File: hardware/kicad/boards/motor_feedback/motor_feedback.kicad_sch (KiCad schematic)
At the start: 65 parts, among them J1 PWM fra MCU, J2 MCP PWM, J3 DC Motor, J4 3-fase ind, J5 3-fase ud, J6 V1 ud til load, Q1 IRF540N, Q2 IRF530, SW1 Switch, U1 MCP601, U10 IL300, U11 MCP601, U2 NE555, U3 ILD74, U4 MCP601, U5 IR2110, U6 LM7805, U7 4N25, U8 IR2110, U9 MCP601

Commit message: motor_feedback: trim to the 8-part isolated amp (3 interface pins pending connectors)
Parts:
- removed C1: 8n2, Capacitor_THT:C_Disc_D5.0mm_W2.5mm_P5.00mm, symbol Device:C
- removed C10, C2, C4, C5, C6: 100n, Capacitor_THT:C_Disc_D5.0mm_W2.5mm_P5.00mm, symbol Device:C
- removed C11: 4700u/50V, Capacitor_THT:CP_Radial_D18.0mm_P7.50mm, symbol Device:C_Polarized
- removed C12: Kondesator terminal, TerminalBlock:TerminalBlock_bornier-2_P5.08mm, symbol Connector:Screw_Terminal_01x02
- removed C3, C8: 22u, Capacitor_THT:CP_Radial_D8.0mm_P3.50mm, symbol Device:C_Polarized
- removed C7, C9: 22u, Capacitor_THT:CP_Radial_D8.0mm_P3.50mm, symbol Device:C
- removed D1, D2: 1N4148, Diode_THT:D_DO-35_SOD27_P7.62mm_Horizontal, symbol Device:D
- removed D10, D11, D5, D6, D8, D9: 1N4006, Diode_THT:D_DO-41_SOD81_P10.16mm_Horizontal, symbol Diode:1N4006
- removed D12: 1N5817, Diode_THT:D_DO-41_SOD81_P10.16mm_Horizontal, symbol Device:D
- removed D3, D4, D7: 1N4007, Diode_THT:D_DO-41_SOD81_P10.16mm_Horizontal, symbol Diode:1N4007
- removed J1: PWM fra MCU, TerminalBlock:TerminalBlock_bornier-2_P5.08mm, symbol Connector:Screw_Terminal_01x02
- removed J2: MCP PWM, Connector_PinHeader_2.54mm:PinHeader_1x02_P2.54mm_Vertical, symbol Connector:Conn_01x02_Socket
- removed J3: DC Motor, TerminalBlock:TerminalBlock_bornier-2_P5.08mm, symbol Connector:Screw_Terminal_01x02
- removed J4: 3-fase ind, TerminalBlock:TerminalBlock_bornier-3_P5.08mm, symbol Connector:Screw_Terminal_01x03
- removed J5: 3-fase ud, TerminalBlock:TerminalBlock_bornier-3_P5.08mm, symbol Connector:Screw_Terminal_01x03
- removed J6: V1 ud til load, TerminalBlock:TerminalBlock_bornier-2_P5.08mm, symbol Connector:Screw_Terminal_01x02
- removed L1: Spole terminal, TerminalBlock:TerminalBlock_bornier-2_P5.08mm, symbol Connector:Screw_Terminal_01x02
- removed Q1: IRF540N, energy_system:TO-220-3_Vertical_LaserPads, symbol Transistor_FET:IRF540N
- removed Q2: IRF530, energy_system:TO-220-3_Vertical_LaserPads, symbol Device:Q_NMOS
- removed R1, R3: 10k, Resistor_THT:R_Axial_DIN0207_L6.3mm_D2.5mm_P7.62mm_Horizontal, symbol Device:R
- removed R10, R11, R13, R2, R6: 1k, Resistor_THT:R_Axial_DIN0207_L6.3mm_D2.5mm_P7.62mm_Horizontal, symbol Device:R
- removed R12, R8: 10, Resistor_THT:R_Axial_DIN0207_L6.3mm_D2.5mm_P7.62mm_Horizontal, symbol Device:R
- removed R4: 515, Resistor_THT:R_Axial_DIN0207_L6.3mm_D2.5mm_P7.62mm_Horizontal, symbol Device:R
- removed R5: 200, Resistor_THT:R_Axial_DIN0207_L6.3mm_D2.5mm_P7.62mm_Horizontal, symbol Device:R
- removed R7, R9: 200R, Resistor_THT:R_Axial_DIN0207_L6.3mm_D2.5mm_P7.62mm_Horizontal, symbol Device:R
- removed RV1: 20k, Potentiometer_THT:Potentiometer_Bourns_3296W_Vertical, symbol Device:R_Potentiometer
- removed RV2: 10k, Potentiometer_THT:Potentiometer_Bourns_3296W_Vertical, symbol Device:R_Potentiometer
- removed SW1: Switch, Button_Switch_THT:SW_DIP_SPSTx02_Slide_9.78x7.26mm_W7.62mm_P2.54mm, symbol Switch:SW_DIP_x02
- removed U1, U4: MCP601, Package_DIP:DIP-8_W7.62mm_LongPads, symbol Amplifier_Operational:MCP601-xP
- removed U2: NE555, Package_DIP:DIP-8_W7.62mm_LongPads, symbol Timer:LM555xM
- removed U3: ILD74, Package_DIP:DIP-8_W7.62mm_LongPads, symbol Isolator:ILD74
- removed U5, U8: IR2110, Package_DIP:DIP-14_W7.62mm_LongPads, symbol Driver_FET:IR2110
- removed U6: LM7805, energy_system:TO-220-3_Vertical_LaserPads, symbol Regulator_Linear:LF50_TO220
- removed U7: 4N25, Package_DIP:DIP-6_W7.62mm_LongPads, symbol Isolator:Optocoupler_DC_PhotoNPN_AKEC
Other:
- note removed: "3-fase ensretter + ladekondensator (gen -> 6x 1N4006 -> ~15 mF -> V1 15 V)"
- note removed: "<-- +5V ~1.1kHz PWM"
- note removed: "Drive Circuit (Exp 3A: PWM -> opto -> IR2110 -> IRF540N -> DC motor)"
- note removed: "Feedback Circuit (Exp 3A: isolated linear amp - MCP601 -> IL300 servo -> MCP601)"
- note removed: "Finjusterer Duty Cycle"
- note removed: "For at forstærke 3.3V til 5V er Av = 1.52 R2 Hvor Av = 1 + ------ R1"
- note removed: "Måler spænding til MCU"

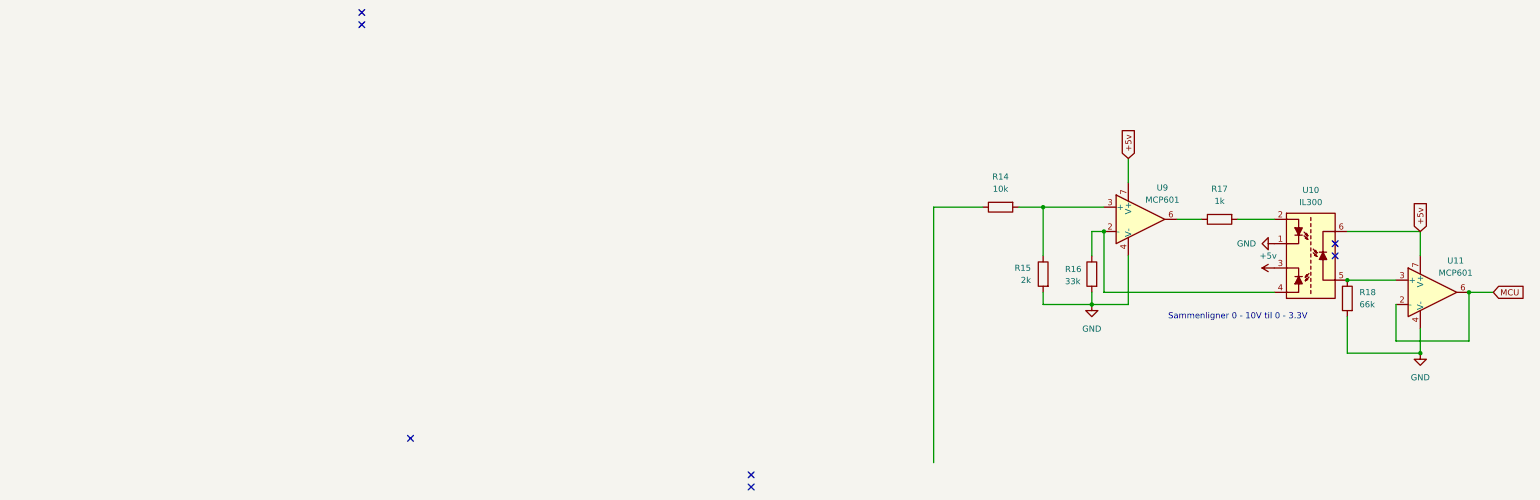
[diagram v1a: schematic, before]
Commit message: motor_feedback: add isolated P1/P2 connectors and power-side ground (ERC 0, barrier intact)
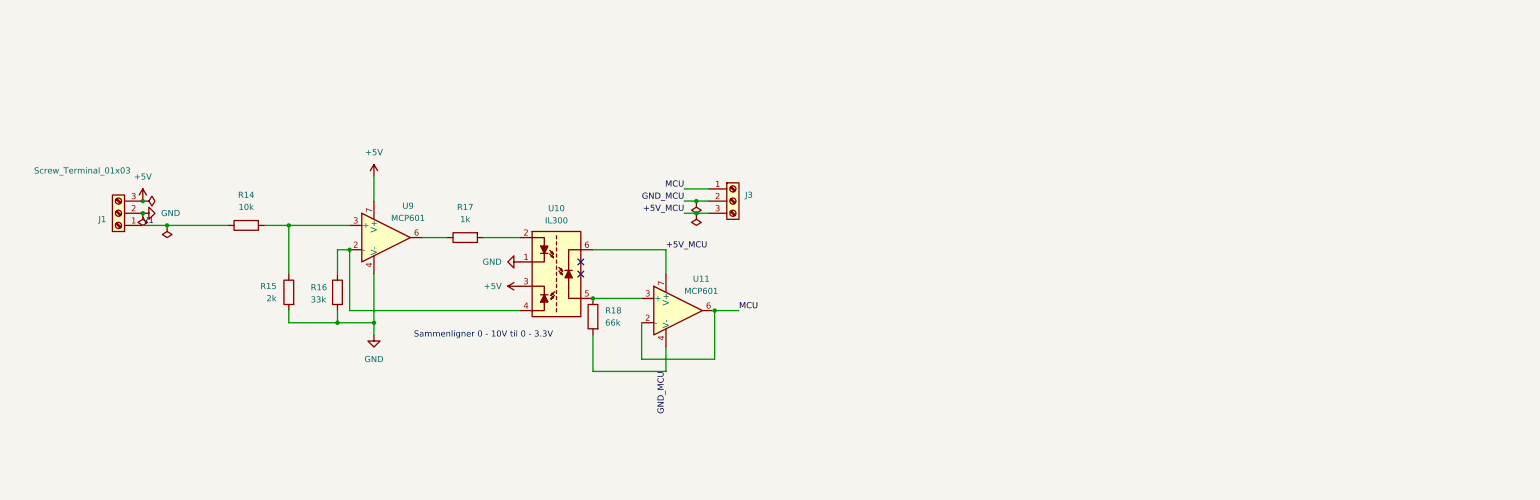
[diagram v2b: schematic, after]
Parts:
- added J1, J3: Screw_Terminal_01x03, TerminalBlock:TerminalBlock_bornier-3_P5.08mm, symbol Connector:Screw_Terminal_01x03
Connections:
- net GND: now also J1.2 (Pin_2); no longer R18.2, U11.4 (V-)
- net MCU: now also J3.1 (Pin_1)
- net V1: now reaches R14.1
- net V1: now also J1.1 (Pin_1)
- net +5v renamed +5V
- net +5V: now also J1.3 (Pin_3); no longer U10.6, U11.7 (V+)
- new net +5V_MCU: J3.3 (Pin_3), U10.6, U11.7 (V+)
- new net GND_MCU: J3.2 (Pin_2), R18.2, U11.4 (V-)
- no-connect marks 7 -> 2
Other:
- moved on the sheet: R14, R15, R16, R17, R18, U10, U11, U9

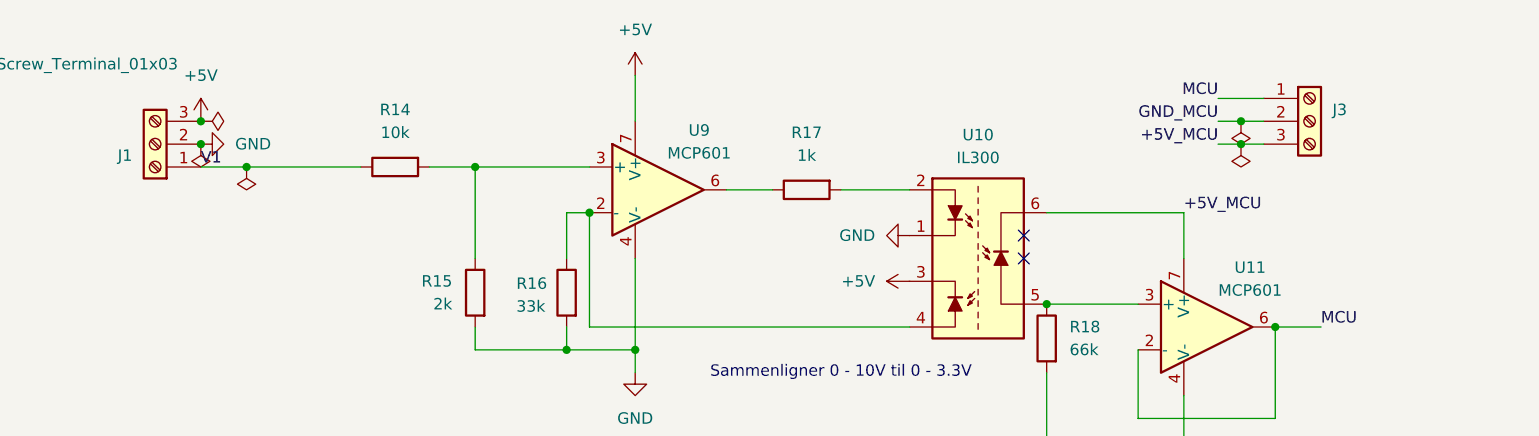
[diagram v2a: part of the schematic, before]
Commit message: system PCB: lock double-sided CNC integration (Phase 0-2.2)
Set up the whole-system board as one double-sided CNC-milled PCB.

- system.kicad_pro: CNC double-sided netclass (clearance 1.0 mm, track 1.0 mm,
  hand-stitch via 2.4/1.0 mm) replacing the laser 0.8 mm rules
- interface contract (docs/superpowers/specs/2026-06-27-...) + rewritten
  label howto for the 5-board split-MCU integration
- split MCU: Arduino owns MPPT (PV INA219 + drives mppt_buck PWM at 5 V),
  C2000 runs motor-buck + boost PID; the two MCUs are fully independent
- current_sense (discrete) dropped; current sensing via PV INA219
- c2000_feedback: strip I-channels + PWM pass, keep 3 V-dividers
  (V1/LOAD/STORE -> ADC)
- hierarchical labels placed on the 5 boards (motor_power, motor_feedback,
  mppt_buck, boost_v2_mill, c2000_feedback) for the system top sheet
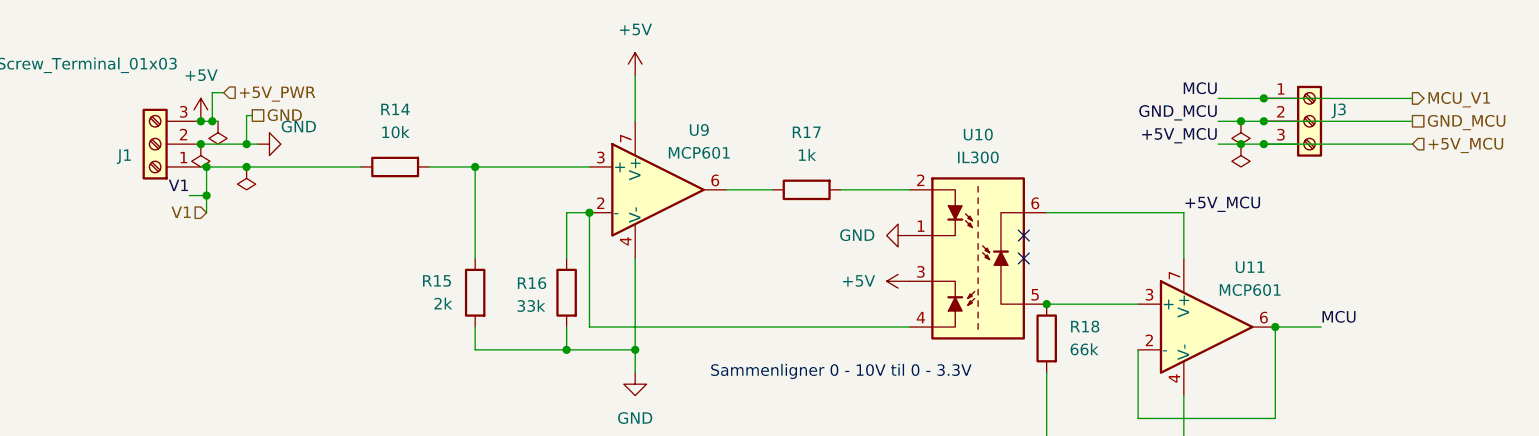
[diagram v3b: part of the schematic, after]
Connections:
- net MCU renamed MCU_V1

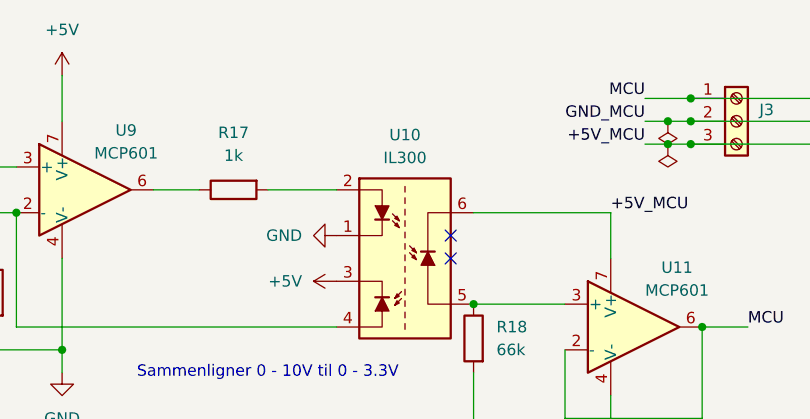
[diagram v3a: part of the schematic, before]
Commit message: system: connected top sheet for the integrated PCB
Rebuild system.kicad_sch as the netlist-connected 5-board hierarchy
(motor_power, motor_feedback, mppt_buck, boost_v2_mill, c2000_feedback),
replacing the old block-diagram. Connectivity by global labels.

- J_ARD (Arduino), J_C2K (C2000), J_INA (PV INA219) connectors
- external screw terminals: 3-phase, motor, PV, store, load, +15V, +5V
- 17 diagnostic probe-point headers on the key nets
- single GND<->GND_MCU star tie (R_STAR 0R)
- generator tools/generators/build_system_top.py (reference; the sheet is
  now hand-maintained in the GUI)

Netlist verified: all 36 top-level connector pins match the interface
contract, no shorts, STORE/V1/LOAD buses span the right boards. Sub-sheet
.kicad_sch carry hierarchical instance data from opening the hierarchy.
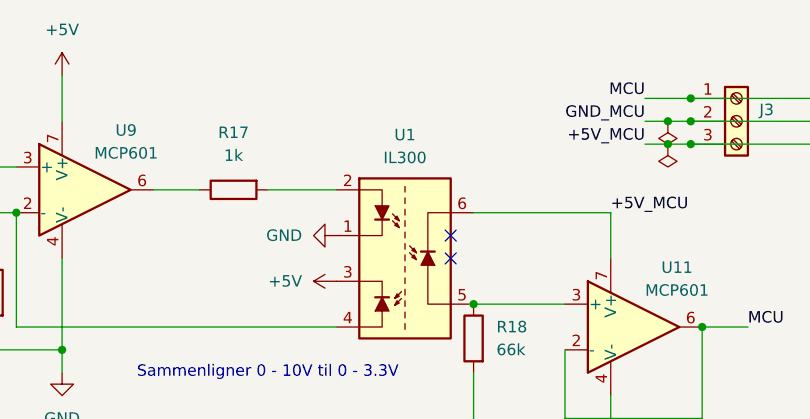
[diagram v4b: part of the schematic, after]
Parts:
- renumbered U10 to U1
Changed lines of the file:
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@@
 		)
 		(instances
+			(project "system"
+				(path "/0b782bdf-68f4-4de8-a396-d6d138d6ad44/b42f1d1b-56f8-4355-881d-b4ff65bc402d"
+					(reference "J3")
+					(unit 1)
+				)
+			)
 			(project "motor_feedback"
 				(path "/b6b31426-5ebe-44be-94a7-40ff693790eb"
@@
 		)
 		(instances
+			(project "system"
+				(path "/0b782bdf-68f4-4de8-a396-d6d138d6ad44/b42f1d1b-56f8-4355-881d-b4ff65bc402d"
+					(reference "#FLG04")
+					(unit 1)
+				)
+			)
 			(project "motor_feedback"
 				(path "/b6b31426-5ebe-44be-94a7-40ff693790eb"
@@
 		)
 		(instances
+			(project "system"
+				(path "/0b782bdf-68f4-4de8-a396-d6d138d6ad44/b42f1d1b-56f8-4355-881d-b4ff65bc402d"
+					(reference "R15")
+					(unit 1)
+				)
+			)
 			(project "motor_feedback"
 				(path "/b6b31426-5ebe-44be-94a7-40ff693790eb"
@@
 		)
 		(instances
+			(project "system"
+				(path "/0b782bdf-68f4-4de8-a396-d6d138d6ad44/b42f1d1b-56f8-4355-881d-b4ff65bc402d"
+					(reference "U9")
+					(unit 1)
+				)
+			)
 			(project "motor_feedback"
 				(path "/b6b31426-5ebe-44be-94a7-40ff693790eb"
@@
 		)
 		(instances
+			(project "system"
+				(path "/0b782bdf-68f4-4de8-a396-d6d138d6ad44/b42f1d1b-56f8-4355-881d-b4ff65bc402d"
+					(reference "#PWR09")
+					(unit 1)
+				)
+			)
 			(project "motor_feedback"
 				(path "/b6b31426-5ebe-44be-94a7-40ff693790eb"
@@
 		)
 		(instances
+			(project "system"
+				(path "/0b782bdf-68f4-4de8-a396-d6d138d6ad44/b42f1d1b-56f8-4355-881d-b4ff65bc402d"
+					(reference "#PWR05")
+					(unit 1)
+				)
+			)
 			(project "motor_feedback"
 				(path "/b6b31426-5ebe-44be-94a7-40ff693790eb"
@@
 		)
 		(instances
+			(project "system"
+				(path "/0b782bdf-68f4-4de8-a396-d6d138d6ad44/b42f1d1b-56f8-4355-881d-b4ff65bc402d"
+					(reference "U11")
+					(unit 1)
+				)
+			)
 			(project "motor_feedback"
 				(path "/b6b31426-5ebe-44be-94a7-40ff693790eb"
@@
 		)
 		(instances
+			(project "system"
+				(path "/0b782bdf-68f4-4de8-a396-d6d138d6ad44/b42f1d1b-56f8-4355-881d-b4ff65bc402d"
+					(reference "#FLG02")
+					(unit 1)
+				)
+			)
 			(project "motor_feedback"
 				(path "/b6b31426-5ebe-44be-94a7-40ff693790eb"
@@
 		)
 		(instances
+			(project "system"
+				(path "/0b782bdf-68f4-4de8-a396-d6d138d6ad44/b42f1d1b-56f8-4355-881d-b4ff65bc402d"
+					(reference "J1")
+					(unit 1)
+				)
+			)
 			(project "motor_feedback"
 				(path "/b6b31426-5ebe-44be-94a7-40ff693790eb"
@@
 		)
 		(instances
+			(project "system"
+				(path "/0b782bdf-68f4-4de8-a396-d6d138d6ad44/b42f1d1b-56f8-4355-881d-b4ff65bc402d"
+					(reference "#PWR01")
+					(unit 1)
+				)
+			)
 			(project "motor_feedback"
 				(path "/b6b31426-5ebe-44be-94a7-40ff693790eb"
@@
 		)
 		(instances
+			(project "system"
+				(path "/0b782bdf-68f4-4de8-a396-d6d138d6ad44/b42f1d1b-56f8-4355-881d-b4ff65bc402d"
+					(reference "#PWR04")
+					(unit 1)
+				)
+			)
 			(project "motor_feedback"
 				(path "/b6b31426-5ebe-44be-94a7-40ff693790eb"
@@
 		)
 		(instances
+			(project "system"
+				(path "/0b782bdf-68f4-4de8-a396-d6d138d6ad44/b42f1d1b-56f8-4355-881d-b4ff65bc402d"
+					(reference "R17")
+					(unit 1)
+				)
+			)
 			(project "motor_feedback"
 				(path "/b6b31426-5ebe-44be-94a7-40ff693790eb"
@@
 		)
 		(instances
+			(project "system"
+				(path "/0b782bdf-68f4-4de8-a396-d6d138d6ad44/b42f1d1b-56f8-4355-881d-b4ff65bc402d"
+					(reference "#PWR02")
+					(unit 1)
+				)
+			)
 			(project "motor_feedback"
 				(path "/b6b31426-5ebe-44be-94a7-40ff693790eb"
@@
 		)
 		(instances
+			(project "system"
+				(path "/0b782bdf-68f4-4de8-a396-d6d138d6ad44/b42f1d1b-56f8-4355-881d-b4ff65bc402d"
+					(reference "#FLG05")
+					(unit 1)
+				)
+			)
 			(project "motor_feedback"
 				(path "/b6b31426-5ebe-44be-94a7-40ff693790eb"
@@
 		)
 		(instances
+			(project "system"
+				(path "/0b782bdf-68f4-4de8-a396-d6d138d6ad44/b42f1d1b-56f8-4355-881d-b4ff65bc402d"
+					(reference "R14")
+					(unit 1)
+				)
+			)
 			(project "motor_feedback"
 				(path "/b6b31426-5ebe-44be-94a7-40ff693790eb"
@@
 		)
 		(instances
+			(project "system"
+				(path "/0b782bdf-68f4-4de8-a396-d6d138d6ad44/b42f1d1b-56f8-4355-881d-b4ff65bc402d"
+					(reference "#FLG03")
+					(unit 1)
+				)
+			)
 			(project "motor_feedback"
 				(path "/b6b31426-5ebe-44be-94a7-40ff693790eb"
@@
 		)
 		(instances
+			(project "system"
+				(path "/0b782bdf-68f4-4de8-a396-d6d138d6ad44/b42f1d1b-56f8-4355-881d-b4ff65bc402d"
+					(reference "R16")
+					(unit 1)
+				)
+			)
 			(project "motor_feedback"
 				(path "/b6b31426-5ebe-44be-94a7-40ff693790eb"
@@
 		)
 		(instances
+			(project "system"
+				(path "/0b782bdf-68f4-4de8-a396-d6d138d6ad44/b42f1d1b-56f8-4355-881d-b4ff65bc402d"
+					(reference "#PWR03")
+					(unit 1)
+				)
+			)
 			(project "motor_feedback"
 				(path "/b6b31426-5ebe-44be-94a7-40ff693790eb"
@@
 		)
 		(instances
+			(project "system"
+				(path "/0b782bdf-68f4-4de8-a396-d6d138d6ad44/b42f1d1b-56f8-4355-881d-b4ff65bc402d"
+					(reference "R18")
+					(unit 1)
+				)
+			)
 			(project "motor_feedback"
 				(path "/b6b31426-5ebe-44be-94a7-40ff693790eb"
@@
 		(in_pos_files yes)
 		(dnp no)
-		(property "Reference" "U10"
+		(property "Reference" "U1"
 			(at 177.8 139.954 0)
 			(show_name no)
@@
 		)
 		(instances
+			(project "system"
+				(path "/0b782bdf-68f4-4de8-a396-d6d138d6ad44/b42f1d1b-56f8-4355-881d-b4ff65bc402d"
+					(reference "U1")
+					(unit 1)
+				)
+			)
 			(project "exp3a"
 				(path "/75e47f2d-71af-4db1-abbe-07e8b83bd23e"
@@
 		)
 		(instances
+			(project "system"
+				(path "/0b782bdf-68f4-4de8-a396-d6d138d6ad44/b42f1d1b-56f8-4355-881d-b4ff65bc402d"
+					(reference "#FLG01")
+					(unit 1)
+				)
+			)
 			(project "motor_feedback"
 				(path "/b6b31426-5ebe-44be-94a7-40ff693790eb"
@@
 		)
 	)
-	(embedded_fonts no)
 )
